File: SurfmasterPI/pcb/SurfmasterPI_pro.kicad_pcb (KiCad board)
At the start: 2 copper layers, 73 parts, among them P1 CLICK_SW, P2 PHONES, P3 BATT_CONN, P4 POWER_SW, P5 THRES, P6 GAIN, P7 COIL, Q1 MPSA13, Q2 IRF9640, Q3 2N3906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

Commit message: Some changes.
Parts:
- removed D2: 1N755, Discret:DO-35
- removed P1: CLICK_SW, Pin_Headers:Pin_Header_Straight_1x02
- removed R5: 22K, Resistors_ThroughHole:Resistor_Horizontal_RM10mm

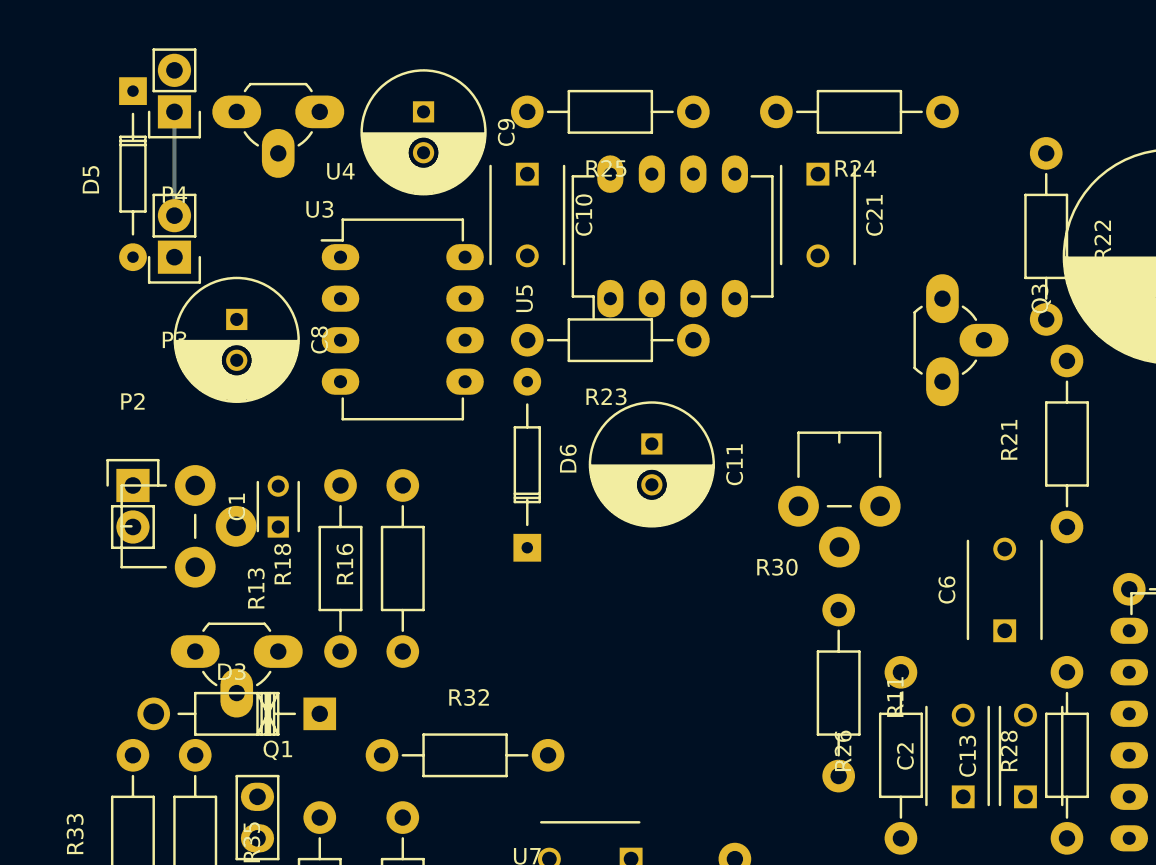
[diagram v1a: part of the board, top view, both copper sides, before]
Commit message: Added patent. Changed TO-92 footprint to compact one.
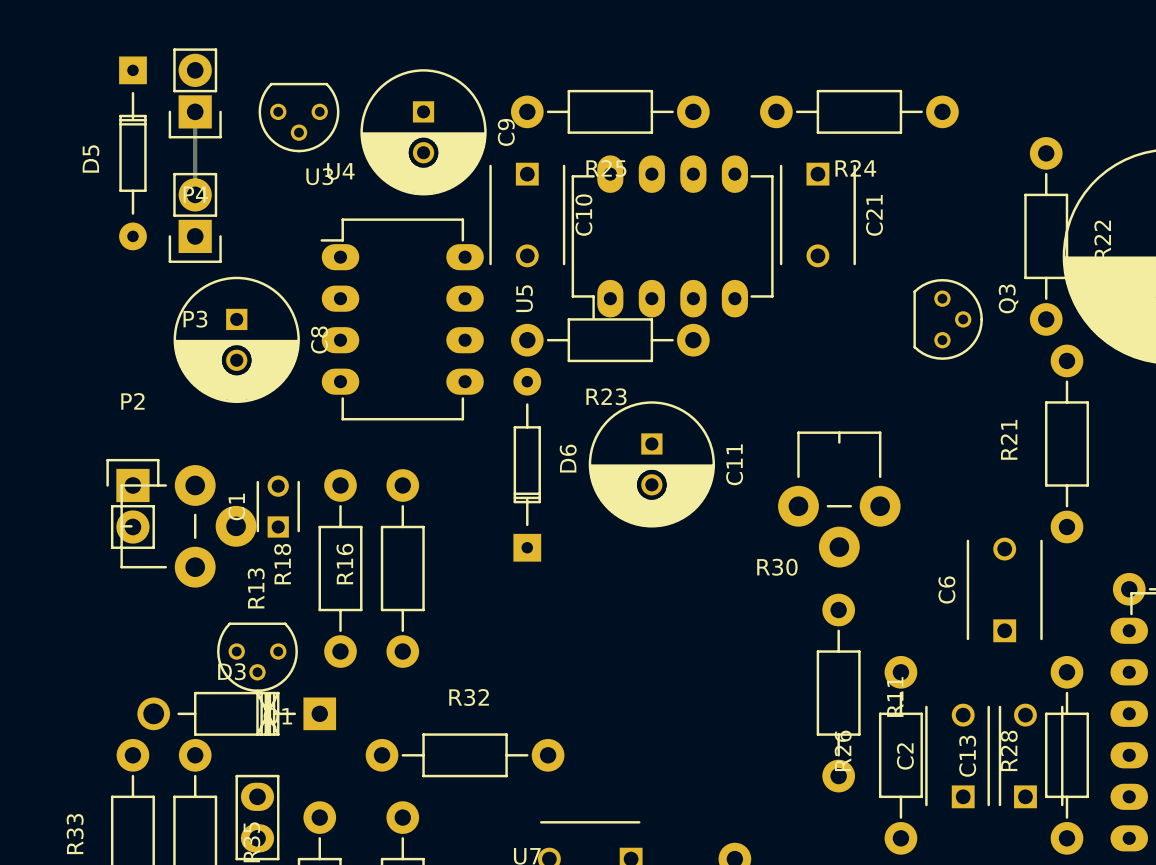
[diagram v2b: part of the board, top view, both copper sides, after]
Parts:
- Q1, Q3, U3: footprint TO_SOT_Packages_THT:TO-92_Rugged -> TO_SOT_Packages_THT:TO-92_Molded_Narrow
- moved P3 1.80 mm to (73.7, 57.1)
- moved D5 1.27 mm to (69.8, 47.0)
- moved P4 1.27 mm to (73.7, 49.5)
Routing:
- net Net-(P3-Pad2): track 6.35 -> 5.08 mm
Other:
- net class Default: trace_width 0.25 -> 0.762

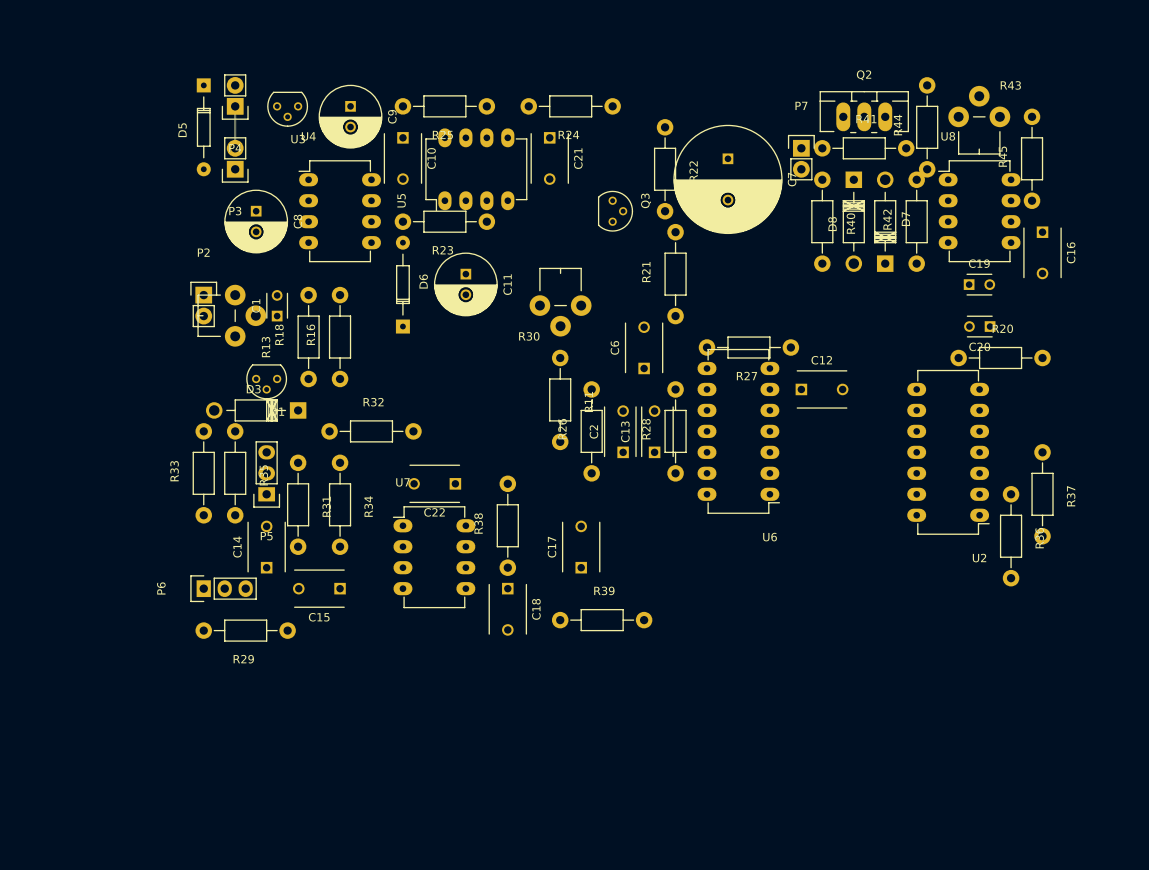
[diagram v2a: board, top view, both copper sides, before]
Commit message: Finished first version of PCB layout for pro.
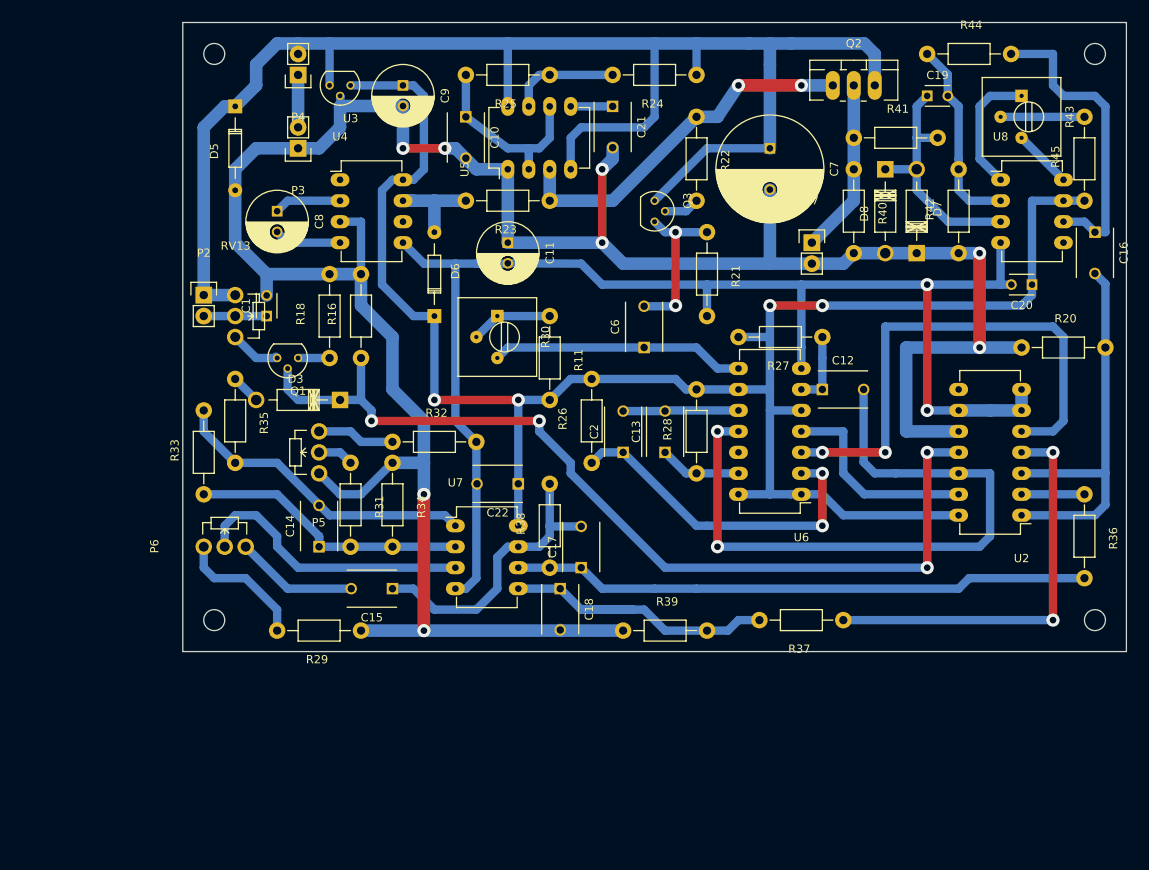
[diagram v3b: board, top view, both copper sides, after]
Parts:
- removed R13: 1K, Potentiometers:Potentiometer_VishaySpectrol-Econtrim-Type36k
- added RV13: 1K, Potentiometers:Potentiometer_WirePads_Small, F.Cu at (73.7, 72.4)
- P5: value THRES -> 10K; footprint Pin_Headers:Pin_Header_Straight_1x03 -> Potentiometers:Potentiometer_WirePads_Small
- P6: value GAIN -> 100K; footprint Pin_Headers:Pin_Header_Straight_1x03 -> Potentiometers:Potentiometer_WirePads_Small
- R30, R43: footprint Potentiometers:Potentiometer_VishaySpectrol-Econtrim-Type36k -> Potentiometers:Potentiometer_Trimmer-Suntan-TSR-3386P
- moved R37 31.5 mm to (147.3, 111.8), turned to 180 degrees
- moved C19 23.4 mm to (157.5, 48.3)
- moved R44 14.0 mm to (157.5, 43.2), turned to 0 degrees
- moved P7 11.5 mm to (143.5, 66.0)
- moved R21 10.9 mm to (130.8, 64.8), turned to 270 degrees
- moved R24 10.9 mm to (129.5, 45.7)
- moved R30 10.2 mm to (105.4, 74.9), turned to 270 degrees
- moved R36 8.89 mm to (176.5, 96.5)
- moved R29 8.89 mm to (88.9, 113.0)
- moved P4 8.52 mm to (81.3, 45.7)
- moved R25 8.52 mm to (111.8, 45.7)
- moved U5 8.52 mm to (106.7, 57.1)
- moved C21 8.52 mm to (119.4, 49.5)
- moved P3 8.03 mm to (81.3, 54.6)
- moved R23 8.03 mm to (111.8, 61.0)
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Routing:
- net GND: track 0.00 -> 306.3 mm, vias 0 -> 8
- net +5V: track 0.00 -> 219.7 mm, vias 0 -> 4
- net +BATT: track 0.00 -> 186.4 mm
- net -5V: track 0.00 -> 166.3 mm, vias 0 -> 2
- net Net-(D3-Pad1): track 0.00 -> 114.0 mm, vias 0 -> 4
- net Net-(C12-Pad2): track 0.00 -> 82.4 mm, vias 0 -> 2
- net Net-(C17-Pad1): track 0.00 -> 70.2 mm
- net Net-(U2-Pad5): track 0.00 -> 63.3 mm, vias 0 -> 2
- net Net-(R37-Pad1): track 0.00 -> 49.5 mm, vias 0 -> 2
- net Net-(C16-Pad2): track 0.00 -> 49.5 mm
- net Net-(Q2-Pad1): track 0.00 -> 44.3 mm, vias 0 -> 2
- net Net-(C2-Pad1): track 0.00 -> 41.0 mm, vias 0 -> 2
- net Net-(C18-Pad1): track 0.00 -> 38.2 mm
- net Net-(C14-Pad2): track 0.00 -> 37.8 mm
- net Net-(C16-Pad1): track 0.00 -> 37.1 mm
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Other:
- board outline added: 114.3 x 76.2 mm
- net class Default: trace_width 0.762 -> 1.016; via_dia 0.6 -> 1.6; via_drill 0.4 -> 0.8
- net class GROUND added: clearance 0.2, trace_width 1.524, via_dia 1.6, via_drill 0.8
- net class POWER added: clearance 0.2, trace_width 1.524, via_dia 1.6, via_drill 0.8

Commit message: Updated PCB holes and pads for low res fabrication.
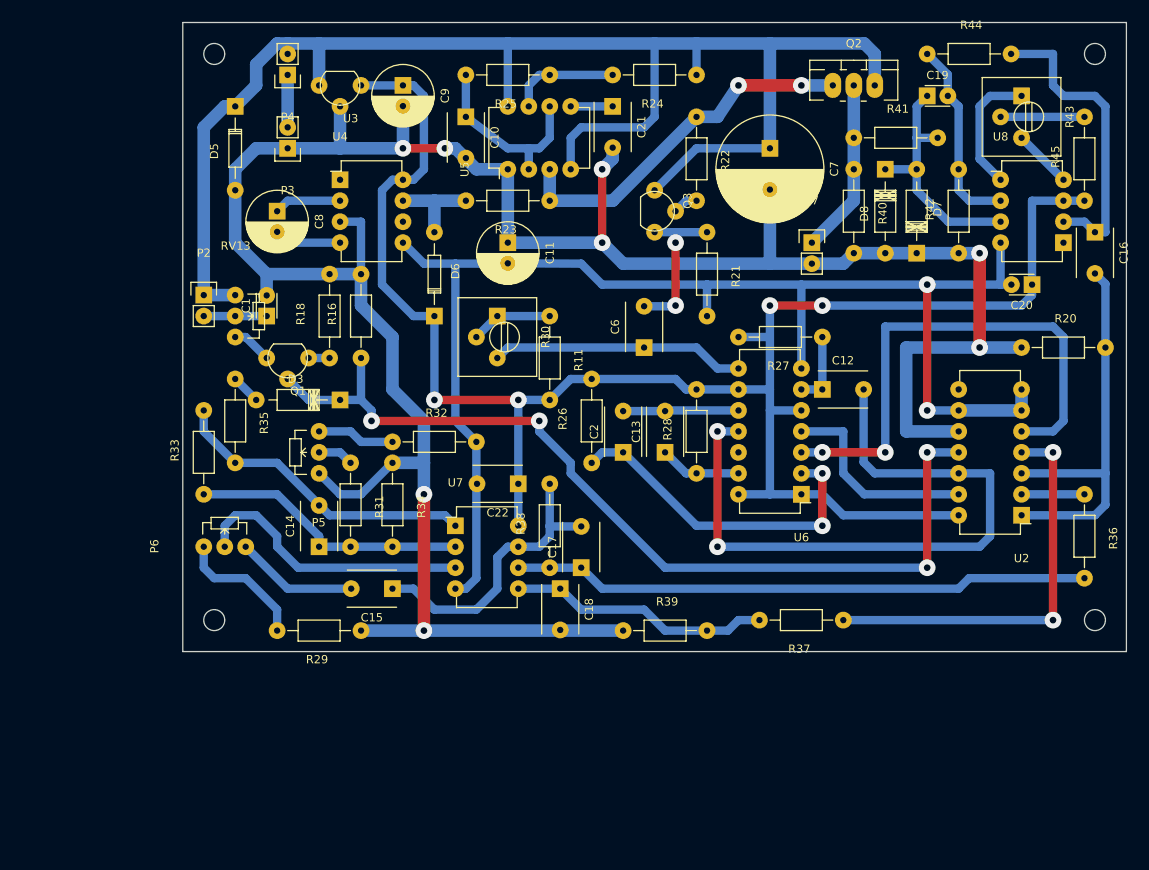
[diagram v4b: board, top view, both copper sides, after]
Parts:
- moved P3 1.27 mm to (80.0, 54.6)
- moved P4 1.27 mm to (80.0, 45.7)
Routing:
- net Net-(C18-Pad1): track 38.2 -> 31.8 mm
- net Net-(D3-Pad1): track 114.0 -> 112.0 mm
- net Net-(Q1-Pad3): track 6.35 -> 4.86 mm
- net +5V: track 219.7 -> 218.4 mm
- net Net-(Q3-Pad2): track 4.34 -> 3.07 mm
- net Net-(Q1-Pad1): track 3.81 -> 2.54 mm
- net Net-(D6-Pad2): track 12.7 -> 11.4 mm
- net +BATT: track 186.4 -> 185.9 mm
- net Net-(C6-Pad2): track 19.6 -> 19.1 mm
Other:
- net class Default: via_dia 1.6 -> 2.032
- net class GROUND: via_dia 1.6 -> 2.032
- net class POWER: via_dia 1.6 -> 2.032

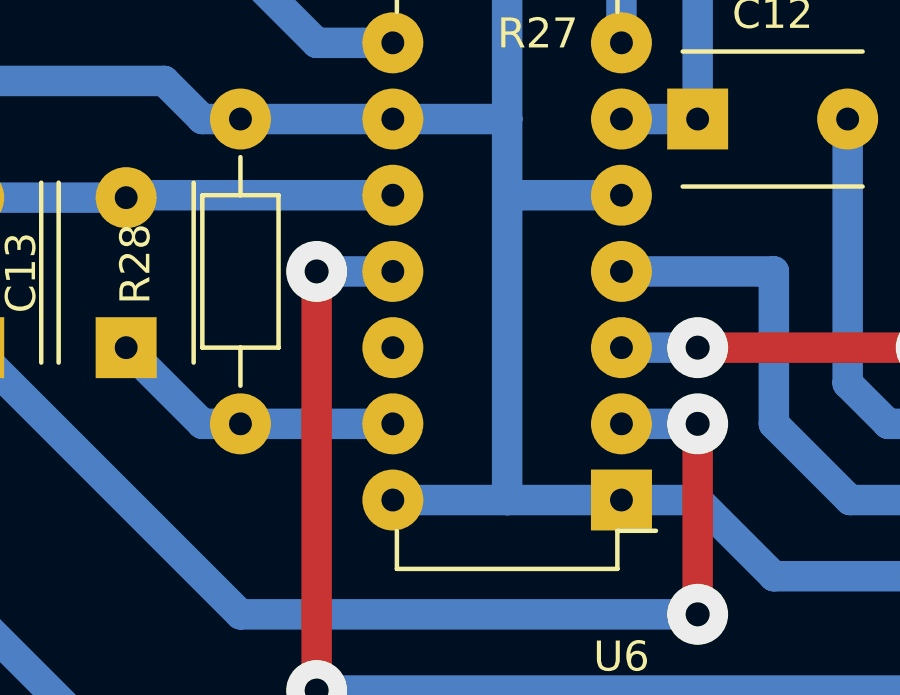
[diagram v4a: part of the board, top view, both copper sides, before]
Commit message: Fixed missing trace from +5 to 4093 pin 12.
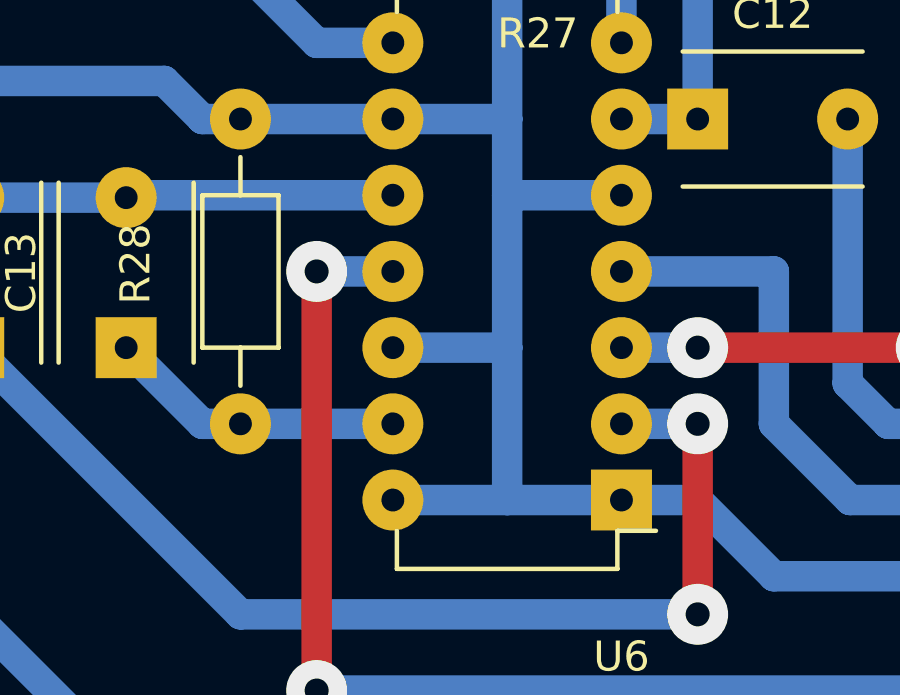
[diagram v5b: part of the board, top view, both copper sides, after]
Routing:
- net +5V: track 218.4 -> 222.2 mm
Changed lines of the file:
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@@
   (general
     (links 145)
-    (no_connects 1)
-    (area 67.234999 39.294999 181.685001 115.645001)
+    (no_connects 0)
+    (area 51.840001 38.70488 182.375 123.350001)
     (thickness 1.6)
     (drawings 22)
-    (tracks 397)
+    (tracks 399)
     (zones 0)
     (modules 70)
@@
   (segment (start 102.87 57.15) (end 106.68 57.15) (width 1.524) (layer B.Cu) (net 1) (status 20))
   (segment (start 80.01 45.72) (end 80.01 52.07) (width 1.524) (layer B.Cu) (net 2) (status 30))
+  (segment (start 138.43 91.44) (end 134.62 91.44) (width 1.016) (layer B.Cu) (net 3) (status 800000))
   (segment (start 173.99 60.96) (end 170.18 60.96) (width 1.016) (layer B.Cu) (net 3) (status 10))
   (segment (start 170.18 60.96) (end 170.18 71.12) (width 1.016) (layer B.Cu) (net 3) (status 20))
@@
   (segment (start 170.18 72.39) (end 170.18 71.12) (width 1.016) (layer B.Cu) (net 3) (status 20))
   (segment (start 168.91 73.66) (end 170.18 72.39) (width 1.016) (layer B.Cu) (net 3))
-  (segment (start 138.43 96.52) (end 138.43 86.36) (width 1.016) (layer B.Cu) (net 3))
+  (segment (start 138.43 96.52) (end 138.43 91.44) (width 1.016) (layer B.Cu) (net 3))
+  (segment (start 138.43 91.44) (end 138.43 86.36) (width 1.016) (layer B.Cu) (net 3))
   (segment (start 138.43 86.36) (end 142.24 86.36) (width 1.016) (layer B.Cu) (net 3) (status 20))
   (segment (start 116.84 82.55) (end 114.3 82.55) (width 1.016) (layer B.Cu) (net 3) (status 10))
